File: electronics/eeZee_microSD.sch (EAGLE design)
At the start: 12 parts, among them U1 MCP1824S, U2 74HC4050, U4 MICROSD_CD

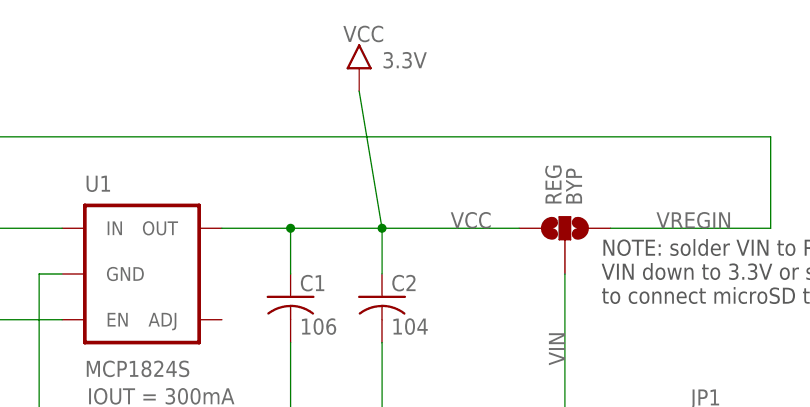
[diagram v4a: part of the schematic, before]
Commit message: Fixed silk error on reg/byp and moved solder jumper
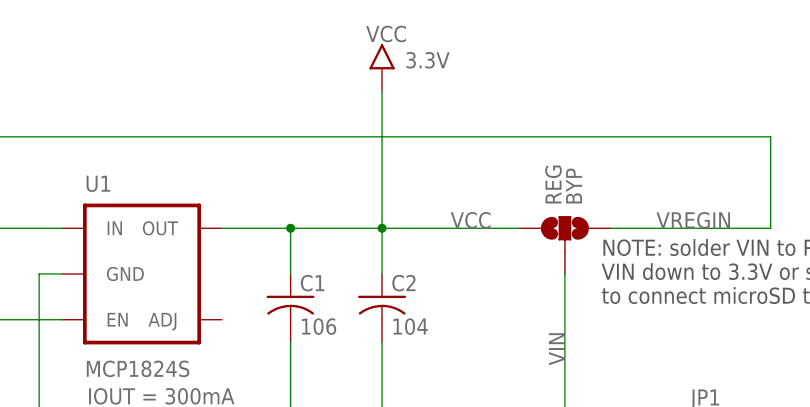
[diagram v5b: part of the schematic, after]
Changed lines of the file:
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@@
 </instance>
 <instance part="GND5" gate="1" x="119.38" y="38.1"/>
-<instance part="U$2" gate="G$1" x="157.48" y="165.1"/>
+<instance part="U$2" gate="G$1" x="160.02" y="165.1"/>
 <instance part="U$3" gate="G$1" x="119.38" y="91.44"/>
 <instance part="U$4" gate="G$1" x="43.18" y="88.9"/>
@@
 <wire x1="160.02" y1="144.78" x2="160.02" y2="149.86" width="0.1524" layer="91"/>
 <pinref part="U$2" gate="G$1" pin="VCC"/>
-<wire x1="160.02" y1="149.86" x2="157.48" y2="165.1" width="0.1524" layer="91"/>
-</segment>
-<segment>
+<wire x1="160.02" y1="149.86" x2="160.02" y2="165.1" width="0.1524" layer="91"/>
+</segment>
+<segment>

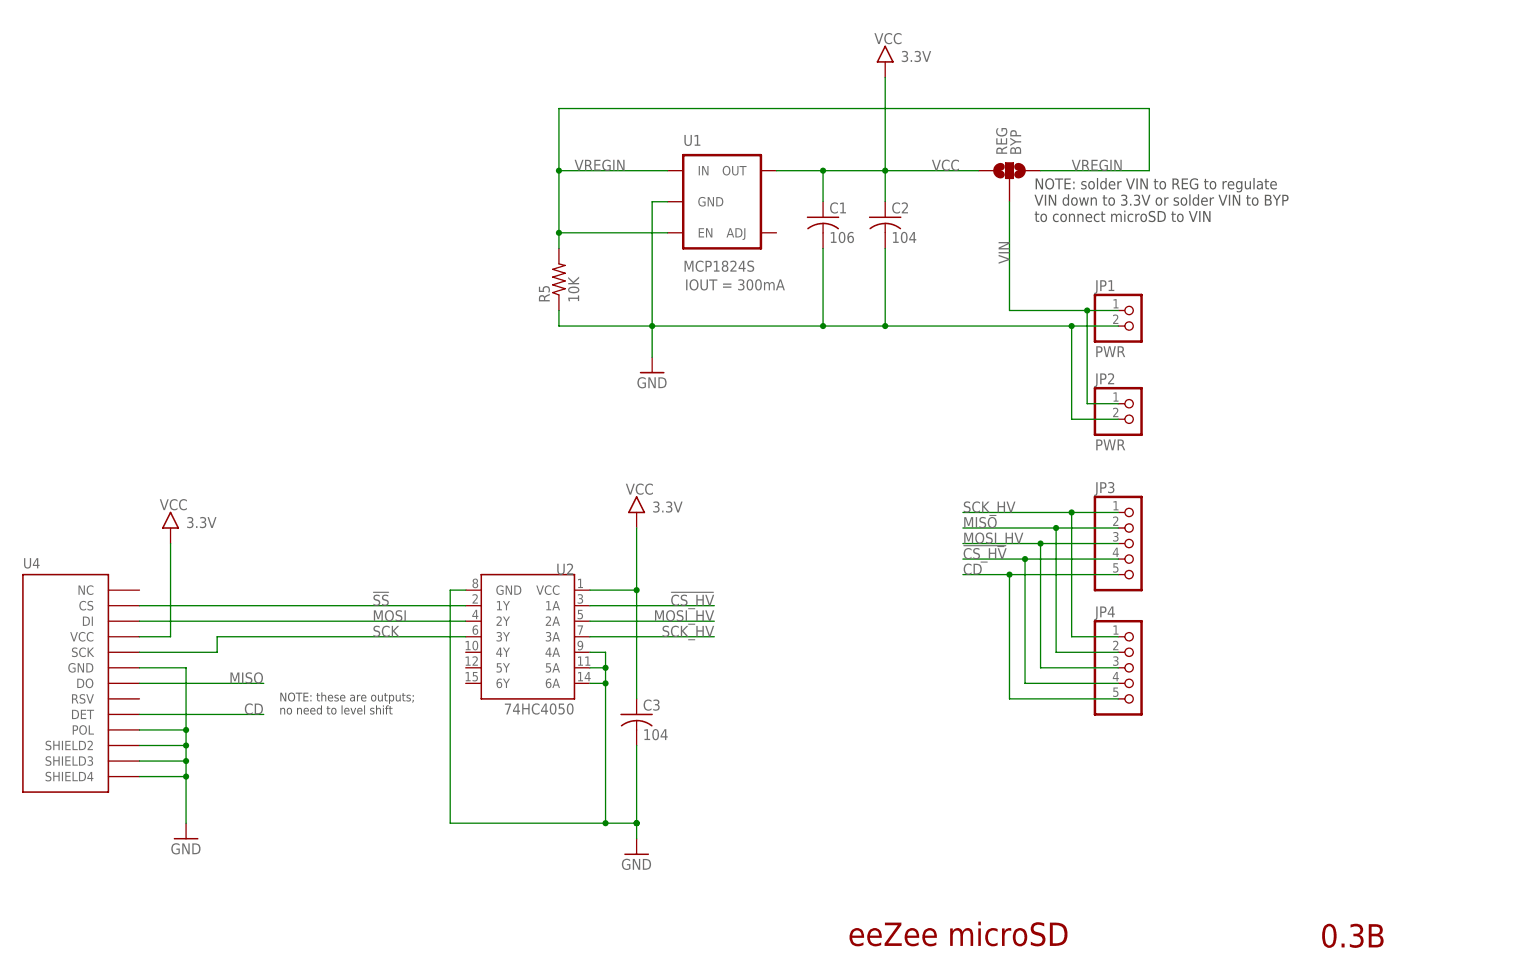
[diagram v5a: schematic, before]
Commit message: Changed solder jumper due to overheat of MCP1824.
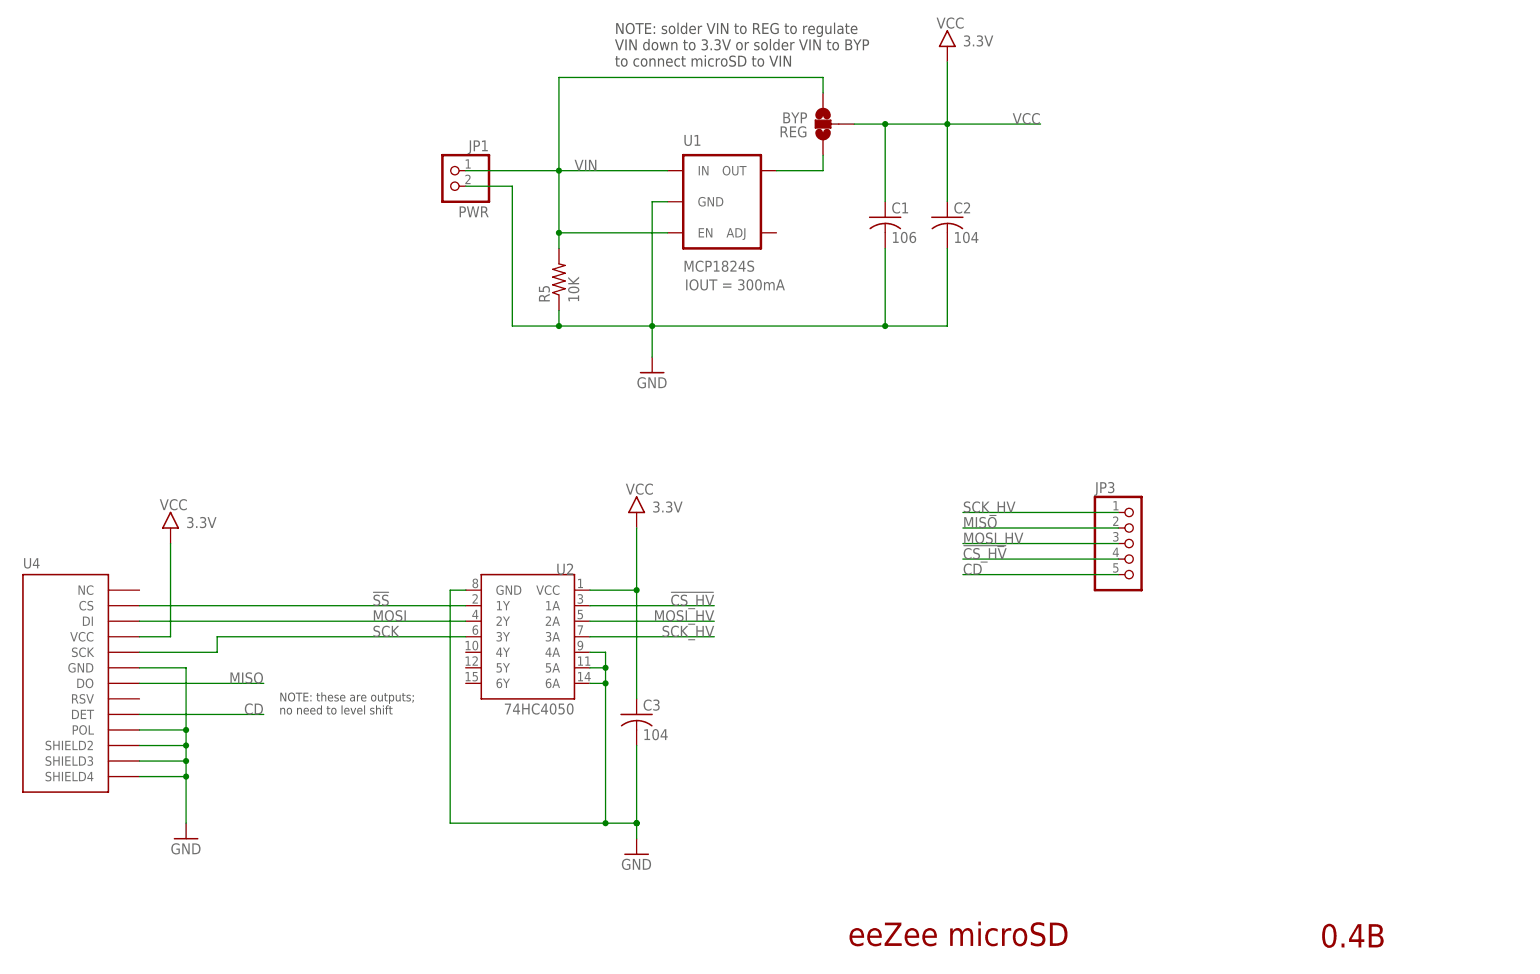
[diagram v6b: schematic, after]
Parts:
- removed JP2: PWR, pinhead-2:PINHD-1X02_2.54-S
- removed JP4: (no value), pinhead-2:PINHD-1X05_2.54-S
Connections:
- removed net VREGIN: R5.2, REG.3, U1.EN, U1.IN
- new net N$1: REG.1, U1.OUT
- net !CS_HV: no longer JP4.4
- net CD: no longer JP4.5
- net GND: no longer JP2.2
- net MISO: no longer JP4.2
- net MOSI_HV: no longer JP4.3
- net SCK_HV: no longer JP4.1
- net VCC: now also REG.2; no longer REG.1, U1.OUT
- net VIN: now also R5.2, REG.3, U1.EN, U1.IN; no longer JP2.1, REG.2
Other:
- note added: "0.4B"
- note removed: "0.3B"
- moved on the sheet: C1, C2, JP1, REG
